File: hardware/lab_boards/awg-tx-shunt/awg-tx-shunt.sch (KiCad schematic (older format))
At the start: 22 parts

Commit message: Added T6003NLT symbol and footprint to awg-tx-shunt.sch to replace the generic transformer originally placed.
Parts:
- removed T? (x3): Transformer_AUDIO, symbol Device:Transformer_AUDIO
- added L? (x3): T6003NL, transformers:T6003NL, symbol T6003NL:T6003NL
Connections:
- wire segments 69 -> 60
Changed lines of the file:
@@
 $EndDescr
-$Comp
-L Device:Transformer_AUDIO T?
-U 1 1 5F5143F4
-P 5600 3250
-F 0 "T?" H 5600 3717 50  0000 C CNN
-F 1 "Transformer_AUDIO" H 5600 3626 50  0000 C CNN
-F 2 "" H 5600 3250 50  0001 C CNN
-F 3 "~" H 5600 3250 50  0001 C CNN
-	1    5600 3250
-	1    0    0    -1
-$EndComp
 $Comp
 L Connector:Conn_Coaxial J?
@@
 F 3 " ~" H 7550 1900 50  0001 C CNN
 	1    7550 1900
-	1    0    0    -1
-$EndComp
-$Comp
-L Device:Transformer_AUDIO T?
-U 1 1 5F5171F7
-P 5600 2100
-F 0 "T?" H 5600 2567 50  0000 C CNN
-F 1 "Transformer_AUDIO" H 5600 2476 50  0000 C CNN
-F 2 "" H 5600 2100 50  0001 C CNN
-F 3 "~" H 5600 2100 50  0001 C CNN
-	1    5600 2100
 	1    0    0    -1
 $EndComp
@@
 	1    0    0    -1
 $EndComp
-$Comp
-L power:GNDPWR #PWR?
-U 1 1 5F52A4F6
-P 4900 3800
-F 0 "#PWR?" H 4900 3600 50  0001 C CNN
-F 1 "GNDPWR" H 4904 3646 50  0000 C CNN
-F 2 "" H 4900 3750 50  0001 C CNN
-F 3 "" H 4900 3750 50  0001 C CNN
-	1    4900 3800
-	1    0    0    -1
-$EndComp
 Wire Wire Line
 	4350 3050 4350 1900
@@
 	4100 2300 4100 3150
 Connection ~ 4100 3150
-$Comp
-L Device:Transformer_AUDIO T?
-U 1 1 5F5338F2
-P 5600 1000
-F 0 "T?" H 5600 1467 50  0000 C CNN
-F 1 "Transformer_AUDIO" H 5600 1376 50  0000 C CNN
-F 2 "" H 5600 1000 50  0001 C CNN
-F 3 "~" H 5600 1000 50  0001 C CNN
-	1    5600 1000
-	1    0    0    -1
-$EndComp
 $Comp
 L Connector:Conn_Coaxial J?
@@
 	1    0    0    -1
 $EndComp
-Wire Wire Line
-	6000 800  6100 800
 $Comp
 L Device:L L?
@@
 	6500 800  6800 800
 Wire Wire Line
-	6000 1200 6100 1200
-Wire Wire Line
 	7550 1200 7550 1000
 $Comp
@@
 	3900 3150 4100 3150
 Wire Wire Line
-	6000 1900 6050 1900
-Wire Wire Line
 	7550 2100 7550 2300
 Wire Wire Line
 	7350 3050 6700 3050
-Wire Wire Line
-	6000 3450 6100 3450
 Wire Wire Line
 	7550 3450 7550 3250
@@
 Connection ~ 4350 1900
 Wire Wire Line
-	6000 2300 6050 2300
-Wire Wire Line
 	6050 2250 6050 2300
 Connection ~ 6050 2300
@@
 Connection ~ 6100 3050
 Wire Wire Line
-	6100 3050 6000 3050
-Wire Wire Line
 	6100 3400 6100 3450
 Connection ~ 6100 3450
@@
 Wire Wire Line
 	6100 1200 7550 1200
-Wire Wire Line
-	5600 1400 5600 1550
-Wire Wire Line
-	5600 1550 4900 1550
-Wire Wire Line
-	4900 1550 4900 2650
-Wire Wire Line
-	5600 3650 5600 3700
-Wire Wire Line
-	5600 3700 4900 3700
-Connection ~ 4900 3700
-Wire Wire Line
-	4900 3700 4900 3800
-Wire Wire Line
-	5600 2500 5600 2650
-Wire Wire Line
-	5600 2650 4900 2650
-Connection ~ 4900 2650
-Wire Wire Line
-	4900 2650 4900 3700
+$Comp
+L T6003NL:T6003NL L?
+U 1 1 5F5801FC
+P 5500 3250
+F 0 "L?" H 5500 3250 50  0001 L BNN
+F 1 "T6003NL" H 5500 3250 50  0001 L BNN
+F 2 "transformers:T6003NL" H 5500 3572 50  0000 C CNN
+F 3 "" H 5500 3250 50  0001 C CNN
+	1    5500 3250
+	1    0    0    -1
+$EndComp
+Wire Wire Line
+	5800 3050 6100 3050
+Wire Wire Line
+	5800 3450 6100 3450
+$Comp
+L T6003NL:T6003NL L?
+U 1 1 5F58D17C
+P 5500 2100
+F 0 "L?" H 5500 2100 50  0001 L BNN
+F 1 "T6003NL" H 5500 2100 50  0001 L BNN
+F 2 "transformers:T6003NL" H 5500 2422 50  0000 C CNN
+F 3 "" H 5500 2100 50  0001 C CNN
+	1    5500 2100
+	1    0    0    -1
+$EndComp
+$Comp
+L T6003NL:T6003NL L?
+U 1 1 5F58F097
+P 5500 1000
+F 0 "L?" H 5500 1000 50  0001 L BNN
+F 1 "T6003NL" H 5500 1000 50  0001 L BNN
+F 2 "transformers:T6003NL" H 5500 1322 50  0000 C CNN
+F 3 "" H 5500 1000 50  0001 C CNN
+	1    5500 1000
+	1    0    0    -1
+$EndComp
+Wire Wire Line
+	5800 800  6100 800
+Wire Wire Line
+	5800 1200 6100 1200
+Wire Wire Line
+	5800 1900 6050 1900
+Wire Wire Line
+	5800 2300 6050 2300
 $EndSCHEMATC

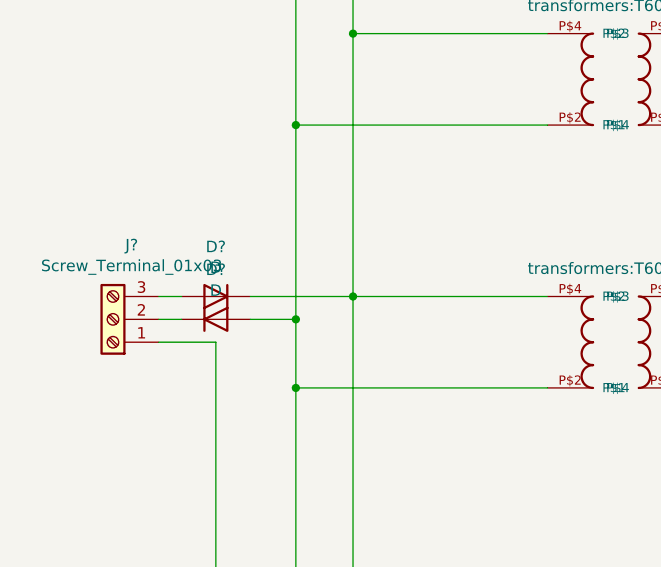
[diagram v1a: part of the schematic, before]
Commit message: added shunt resistor footprint.
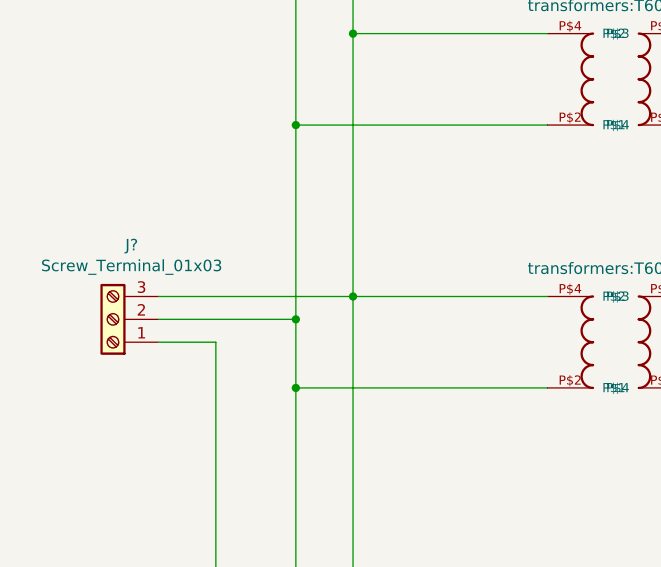
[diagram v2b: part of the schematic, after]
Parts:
- removed D? (x2): D, symbol Device:D
- R?: footprint (none) -> Resistor_SMD:R_Shunt_Vishay_WSK2512_6332Metric_T1.19mm
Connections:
- net at L?.P$4 (P$2), L?.P$4 (P$2), L?.P$4 (P$2)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: now also J?.3 (Pin_3)
- net at J?.2 (Pin_2): now also J?.2 (Ext), L?.P$2 (P$1), L?.P$2 (P$1), L?.P$2 (P$1)
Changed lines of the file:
@@
 F 0 "R?" V 5517 5550 50  0000 C CNN
 F 1 "R_Shunt_US" V 5426 5550 50  0000 C CNN
-F 2 "" V 5580 5550 50  0001 C CNN
+F 2 "Resistor_SMD:R_Shunt_Vishay_WSK2512_6332Metric_T1.19mm" V 5580 5550 50  0001 C CNN
 F 3 "~" H 5650 5550 50  0001 C CNN
 	1    5650 5550
@@
 	4350 5550 4350 3050
 Wire Wire Line
-	4350 3050 3900 3050
-Wire Wire Line
-	3500 3150 3600 3150
-Wire Wire Line
 	4100 3150 4100 3450
 Wire Wire Line
@@
 Wire Wire Line
 	7550 1200 7550 1000
-$Comp
-L Device:D D?
-U 1 1 5F53D070
-P 3750 3050
-F 0 "D?" H 3750 2833 50  0000 C CNN
-F 1 "D" H 3750 2924 50  0000 C CNN
-F 2 "" H 3750 3050 50  0001 C CNN
-F 3 "~" H 3750 3050 50  0001 C CNN
-	1    3750 3050
-	-1   0    0    1
-$EndComp
-Wire Wire Line
-	3600 3050 3500 3050
-$Comp
-L Device:D D?
-U 1 1 5F53D5F2
-P 3750 3150
-F 0 "D?" H 3750 3367 50  0000 C CNN
-F 1 "D" H 3750 3276 50  0000 C CNN
-F 2 "" H 3750 3150 50  0001 C CNN
-F 3 "~" H 3750 3150 50  0001 C CNN
-	1    3750 3150
-	1    0    0    -1
-$EndComp
-Wire Wire Line
-	3900 3150 4100 3150
 Wire Wire Line
 	7550 2100 7550 2300
@@
 Wire Wire Line
 	5800 2300 6050 2300
+Wire Wire Line
+	3500 3050 4350 3050
+Wire Wire Line
+	3500 3150 4100 3150
 $EndSCHEMATC

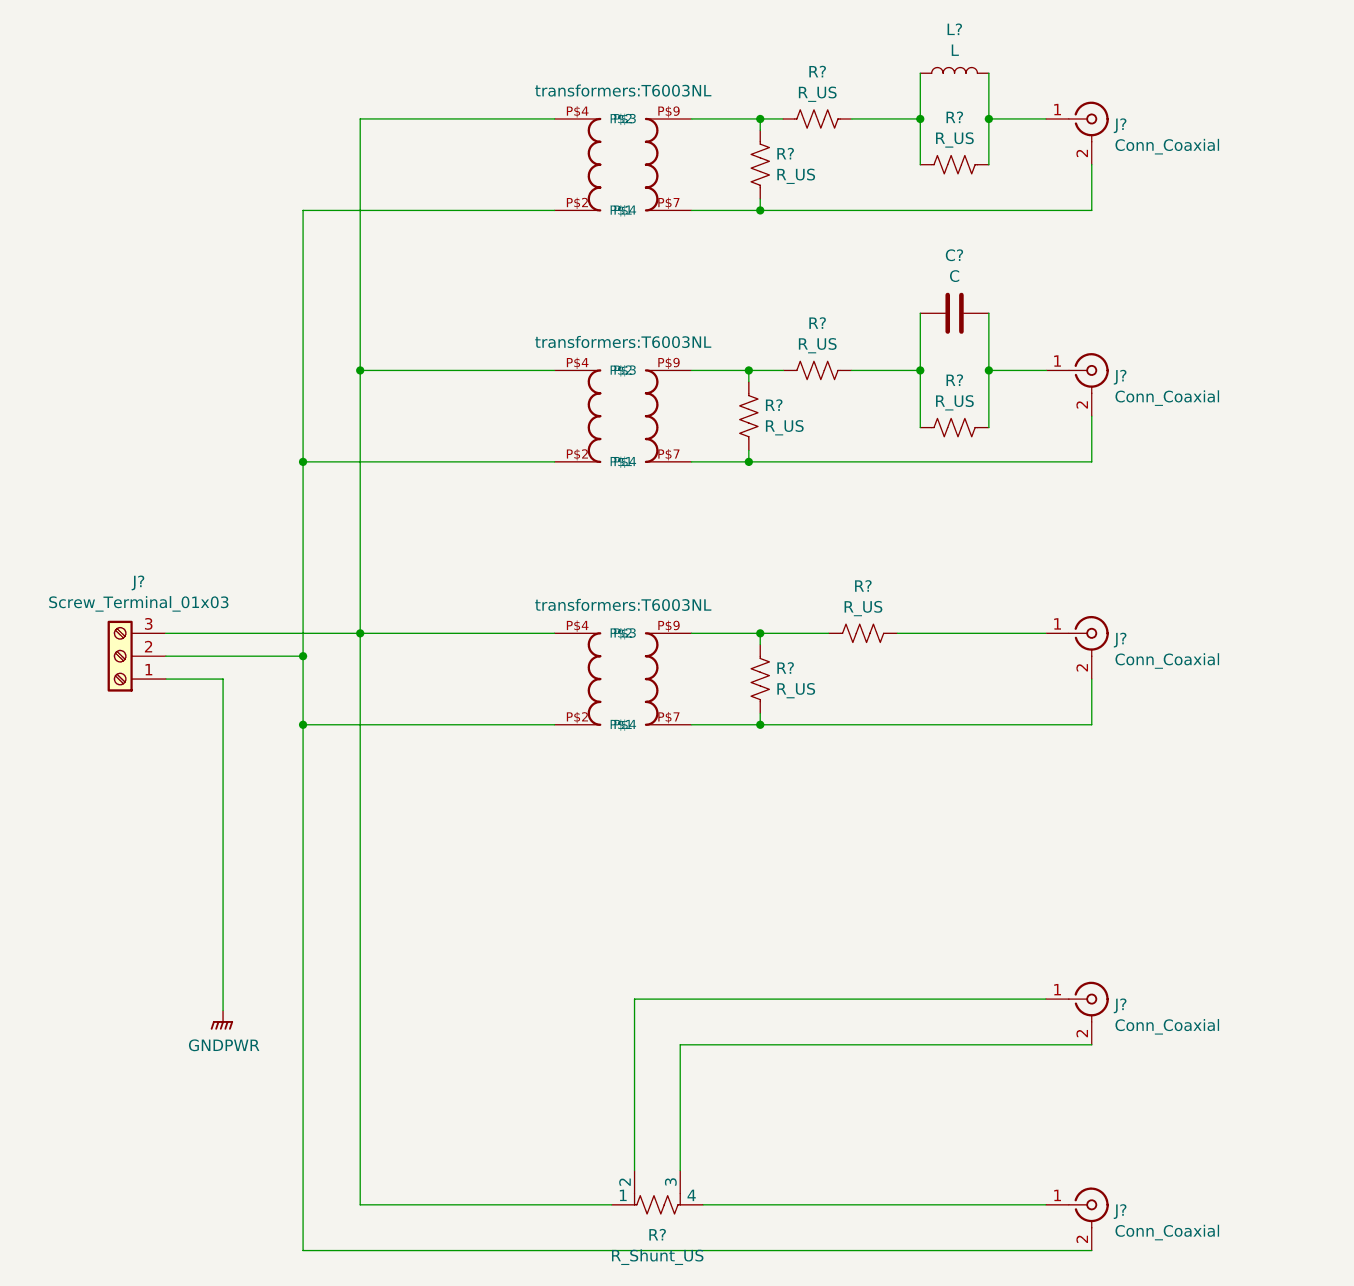
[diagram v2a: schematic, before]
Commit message: Reworked the TX routing board and transformer PCB layout. Simplified by removing calibration circuitry, which will be in a separate board design. Added test points.
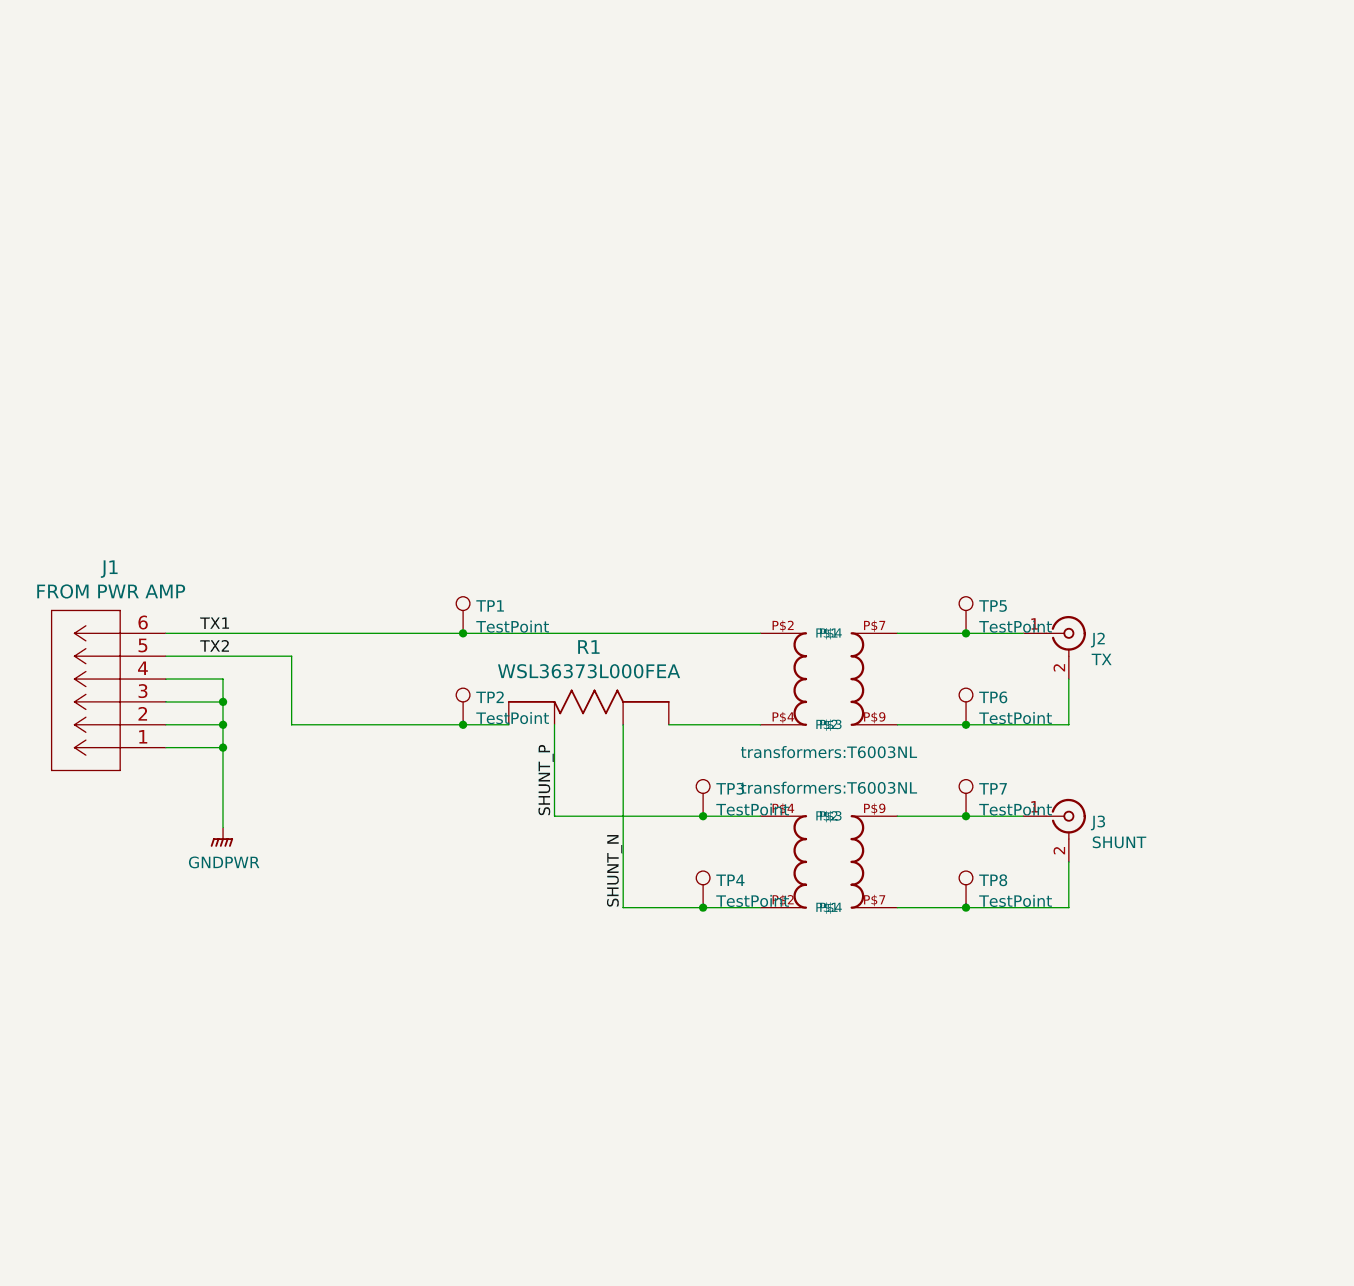
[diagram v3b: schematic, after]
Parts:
- removed C?: C, symbol Device:C
- removed J? (x4): Conn_Coaxial, symbol Connector:Conn_Coaxial
- removed J?: Screw_Terminal_01x03, symbol Connector:Screw_Terminal_01x03
- removed L?: L, symbol Device:L
- removed L? (x2): T6003NL, transformers:T6003NL, symbol T6003NL:T6003NL
- removed R?: R_Shunt_US, Resistor_SMD:R_Shunt_Vishay_WSK2512_6332Metric_T1.19mm, symbol Device:R_Shunt_US
- removed R? (x8): R_US, symbol Device:R_US
- added J1: FROM PWR AMP, phoenix-6pos-1984659:1984659, symbol phoenix-6pos-1984659:1984659
- added J2: TX, Connector_Coaxial:BNC_Amphenol_B6252HB-NPP3G-50_Horizontal, symbol Connector:Conn_Coaxial
- added L2: T6003NL, transformers:T6003NL, symbol T6003NL:T6003NL
- added R1: WSL36373L000FEA, WSL36373L000FEA:WSL36373L000FEA, symbol WSL36373L000FEA:WSL36373L000FEA
- added TP1, TP2, TP3, TP4, TP5, TP6, TP7, TP8: TestPoint, TestPoint:TestPoint_Pad_D4.0mm, symbol Connector:TestPoint
- J3: renamed from J?; value Conn_Coaxial -> SHUNT; footprint (none) -> Connector_Coaxial:BNC_Amphenol_B6252HB-NPP3G-50_Horizontal
- gave numbers to parts that had none: 1
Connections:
- net GNDPWR: now also J1.1, J1.2, J1.3, J1.4
- net at L1.P$4 (P$2): now also R1.1
- net at J3.1 (In): now also L2.P$9 (P$3), TP7.1
- net at J3.2 (Ext): now also L2.P$7 (P$4), TP8.1
- net TX1: now reaches L1.P$2 (P$1)
- net TX1: now also J1.6, TP1.1
- net at L1.P$7 (P$4): now also J2.1 (In), TP5.1
- net at L1.P$9 (P$3): now also J2.2 (Ext), TP6.1
- new net SHUNT_N: L2.P$2 (P$1), R1.2, TP4.1
- new net SHUNT_P: L2.P$4 (P$2), R1.3, TP3.1
- new net TX2: J1.5, R1.4, TP2.1
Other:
- moved on the sheet: J3

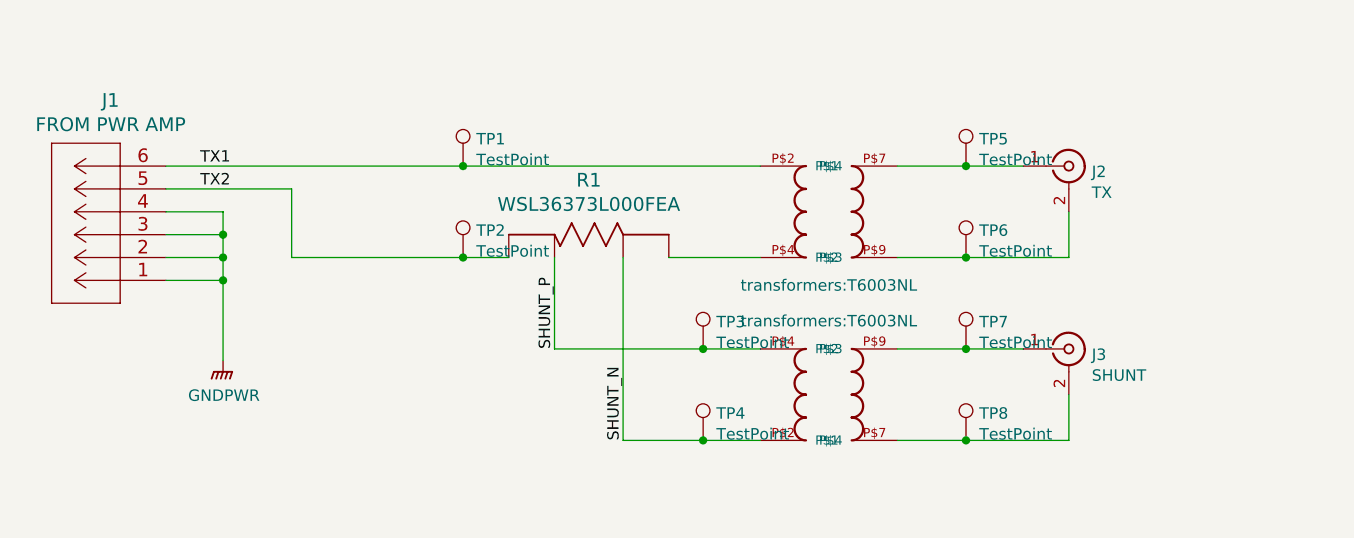
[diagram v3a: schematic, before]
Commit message: Revisions to awg-shunt-tx.sch shunt resistor.
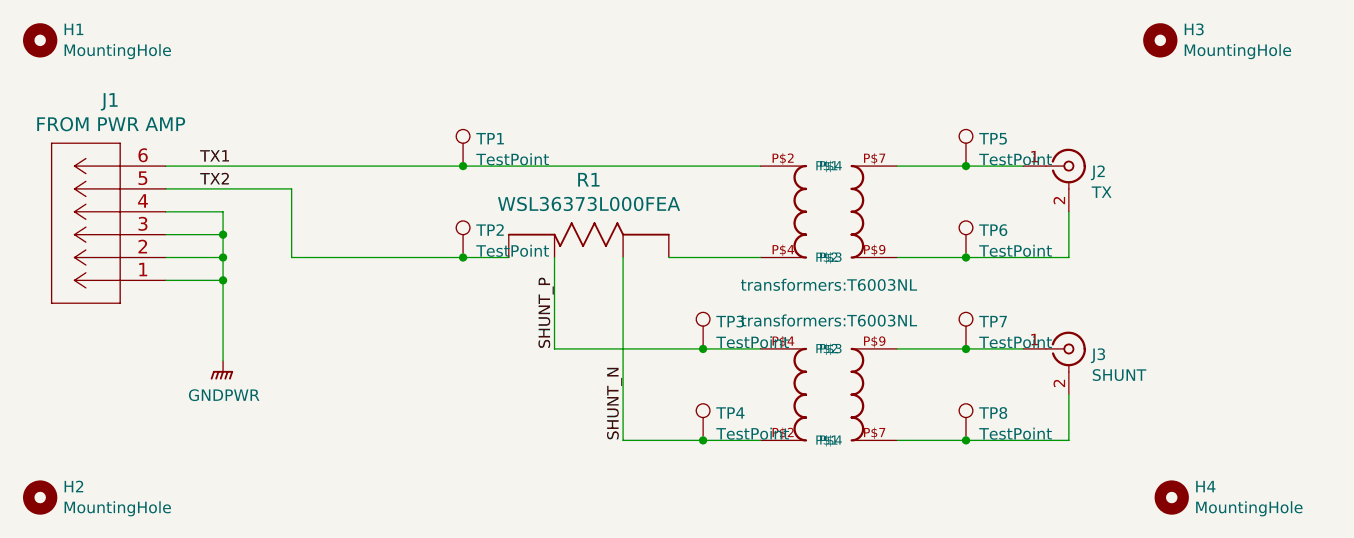
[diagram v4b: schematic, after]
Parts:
- added H1, H2, H3, H4: MountingHole, MountingHole:MountingHole_3.2mm_M3_Pad_Via, symbol Mechanical:MountingHole
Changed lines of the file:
@@
 Text Label 5500 4250 1    50   ~ 0
 SHUNT_N
+$Comp
+L Mechanical:MountingHole H3
+U 1 1 5F60CBBC
+P 7850 2500
+F 0 "H3" H 7950 2546 50  0000 L CNN
+F 1 "MountingHole" H 7950 2455 50  0000 L CNN
+F 2 "MountingHole:MountingHole_3.2mm_M3_Pad_Via" H 7850 2500 50  0001 C CNN
+F 3 "~" H 7850 2500 50  0001 C CNN
+	1    7850 2500
+	1    0    0    -1
+$EndComp
+$Comp
+L Mechanical:MountingHole H4
+U 1 1 5F60D012
+P 7900 4500
+F 0 "H4" H 8000 4546 50  0000 L CNN
+F 1 "MountingHole" H 8000 4455 50  0000 L CNN
+F 2 "MountingHole:MountingHole_3.2mm_M3_Pad_Via" H 7900 4500 50  0001 C CNN
+F 3 "~" H 7900 4500 50  0001 C CNN
+	1    7900 4500
+	1    0    0    -1
+$EndComp
+$Comp
+L Mechanical:MountingHole H1
+U 1 1 5F60D416
+P 2950 2500
+F 0 "H1" H 3050 2546 50  0000 L CNN
+F 1 "MountingHole" H 3050 2455 50  0000 L CNN
+F 2 "MountingHole:MountingHole_3.2mm_M3_Pad_Via" H 2950 2500 50  0001 C CNN
+F 3 "~" H 2950 2500 50  0001 C CNN
+	1    2950 2500
+	1    0    0    -1
+$EndComp
+$Comp
+L Mechanical:MountingHole H2
+U 1 1 5F60E242
+P 2950 4500
+F 0 "H2" H 3050 4546 50  0000 L CNN
+F 1 "MountingHole" H 3050 4455 50  0000 L CNN
+F 2 "MountingHole:MountingHole_3.2mm_M3_Pad_Via" H 2950 4500 50  0001 C CNN
+F 3 "~" H 2950 4500 50  0001 C CNN
+	1    2950 4500
+	1    0    0    -1
+$EndComp
 $EndSCHEMATC
